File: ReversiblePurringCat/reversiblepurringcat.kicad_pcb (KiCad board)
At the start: 2 copper layers, 116 x 90.9 mm, 34 parts, among them J0 nice!view, U0 ProMicro-kbd

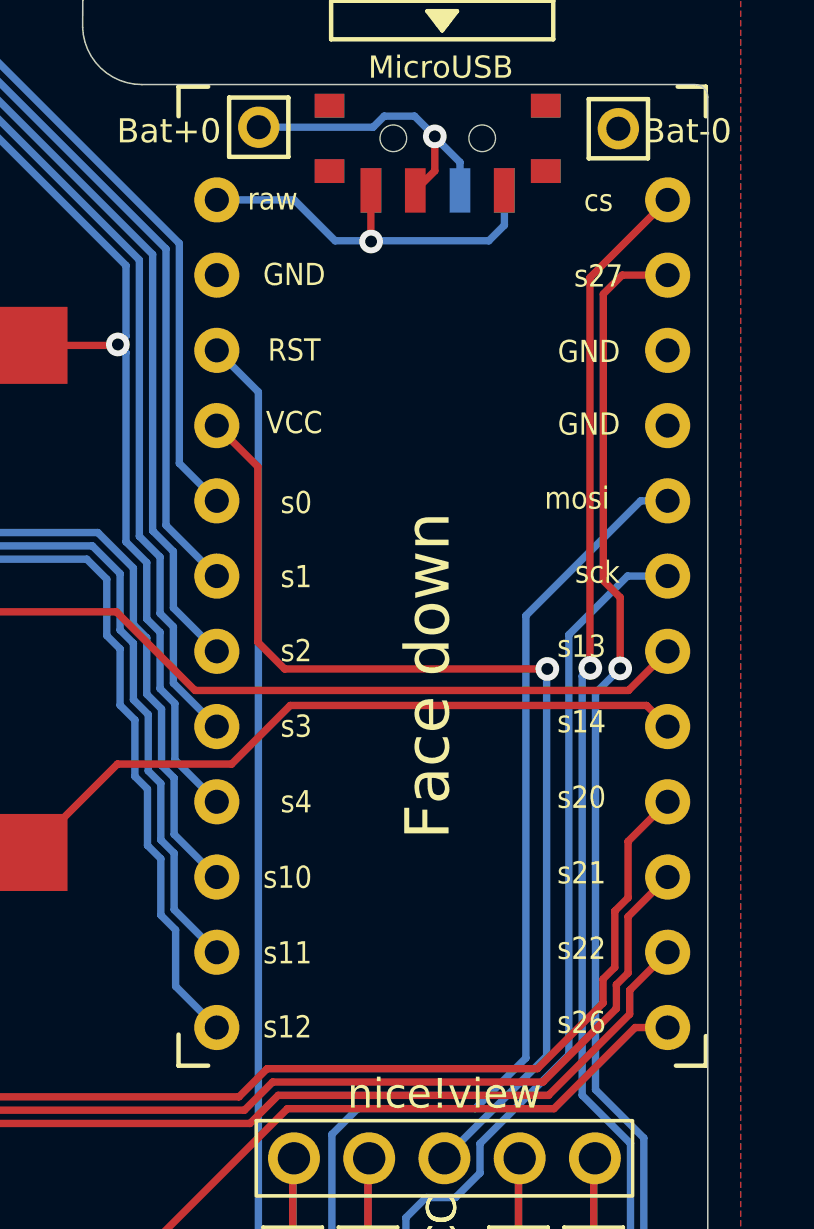
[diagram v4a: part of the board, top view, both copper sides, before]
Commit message: updated labels
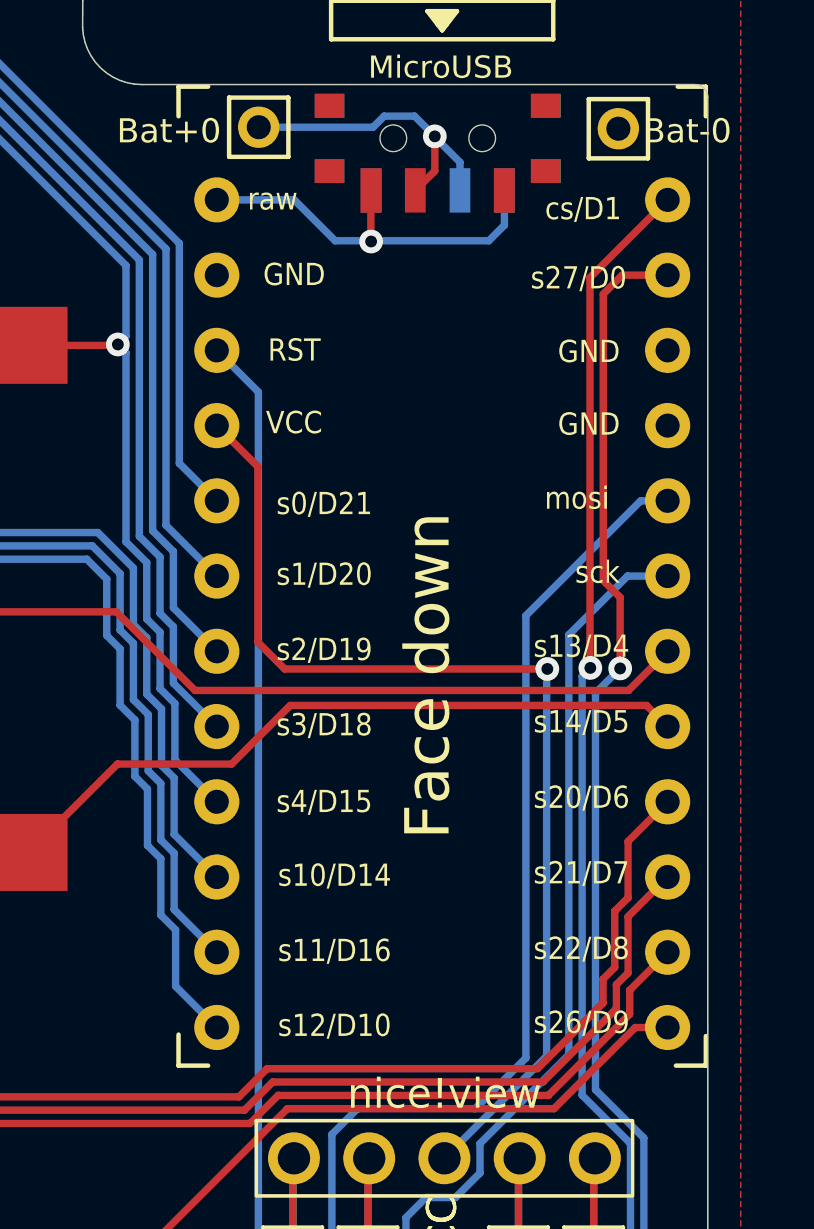
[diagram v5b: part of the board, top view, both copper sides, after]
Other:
- board text added: "s14/D5"
- board text removed: "s14"
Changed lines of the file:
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@@
 			)
 		)
-		(fp_text user "s22"
+		(fp_text user "s22/D8"
 			(at 4.705 10.8 0)
 			(unlocked yes)
@@
 			)
 		)
-		(fp_text user "s2"
-			(at -4.395 0.75 0)
+		(fp_text user "s2/D19"
+			(at -2.35184 0.710728 0)
 			(unlocked yes)
 			(layer "F.SilkS")
@@
 			)
 		)
-		(fp_text user "cs"
-			(at 5.27576 -14.45 0)
+		(fp_text user "cs/D1"
+			(at 4.76016 -14.173672 0)
 			(unlocked yes)
 			(layer "F.SilkS")
@@
 			)
 		)
-		(fp_text user "s3"
-			(at -4.395 3.3 0)
+		(fp_text user "s3/D18"
+			(at -2.35184 3.250728 0)
 			(unlocked yes)
 			(layer "F.SilkS")
@@
 			)
 		)
-		(fp_text user "s27"
-			(at 5.27576 -11.9 0)
+		(fp_text user "s27/D0"
+			(at 4.60776 -11.836872 0)
 			(unlocked yes)
 			(layer "F.SilkS")
@@
 			)
 		)
-		(fp_text user "s10"
-			(at -4.395 8.4 0)
+		(fp_text user "s10/D14"
+			(at -1.713745 8.330728 0)
 			(unlocked yes)
 			(layer "F.SilkS")
@@
 			)
 		)
-		(fp_text user "s11"
-			(at -4.395 10.95 0)
+		(fp_text user "s11/D16"
+			(at -1.713745 10.870728 0)
 			(unlocked yes)
 			(layer "F.SilkS")
@@
 			)
 		)
-		(fp_text user "s12"
-			(at -4.395 13.45 0)
+		(fp_text user "s12/D10"
+			(at -1.713745 13.3992 0)
 			(unlocked yes)
 			(layer "F.SilkS")
@@
 			)
 		)
-		(fp_text user "s26"
+		(fp_text user "s26/D9"
 			(at 4.705 13.3 0)
 			(unlocked yes)
@@
 			)
 		)
-		(fp_text user "s4"
-			(at -4.395 5.85 0)
+		(fp_text user "s4/D15"
+			(at -2.35184 5.841528 0)
 			(unlocked yes)
 			(layer "F.SilkS")
@@
 			)
 		)
-		(fp_text user "s0"
-			(at -4.395 -4.25 0)
+		(fp_text user "s0/D21"
+			(at -2.35184 -4.216872 0)
 			(unlocked yes)
 			(layer "F.SilkS")
@@
 			)
 		)
-		(fp_text user "s21"
+		(fp_text user "s21/D7"
 			(at 4.705 8.25 0)
 			(unlocked yes)
@@
 			)
 		)
-		(fp_text user "s20"
+		(fp_text user "s20/D6"
 			(at 4.705 5.7 0)
 			(unlocked yes)
@@
 			)
 		)
-		(fp_text user "s1"
-			(at -4.395 -1.75 0)
+		(fp_text user "s1/D20"
+			(at -2.35184 -1.829272 0)
 			(unlocked yes)
 			(layer "F.SilkS")
@@
 			)
 		)
-		(fp_text user "s13"
+		(fp_text user "s13/D4"
 			(at 4.705 0.6 0)
 			(unlocked yes)
@@
 		)
 		(fp_line
-			(start -6.999999 -6)
+			(start -6.999998 -6)
 			(end -7 -7)
 			(stroke
@@
 		)
 		(fp_line
-			(start -6 6.999999)
+			(start -6 6.999998)
 			(end -7 7)
 			(stroke
@@
 		(fp_line
 			(start 1.5 3.7)
-			(end -0.999999 3.7)
+			(end -0.999998 3.7)
 			(stroke
 				(width 0.15)
@@
 		)
 		(fp_line
-			(start 6 -6.999999)
+			(start 6 -6.999998)
 			(end 7 -7)
 			(stroke
@@
 		)
 		(fp_line
-			(start 6.999999 6)
+			(start 6.999998 6)
 			(end 7 7)
 			(stroke
@@
 		)
 		(fp_arc
-			(start -0.999999 3.7)
+			(start -0.999998 3.7)
 			(mid -2.060659 3.26066)
 			(end -2.5 2.2)
@@
 		)
 		(fp_line
-			(start -6.999999 -6)
+			(start -6.999998 -6)
 			(end -7 -7)
 			(stroke
@@
 		)
 		(fp_line
-			(start -6 6.999999)
+			(start -6 6.999998)
 			(end -7 7)
 			(stroke
@@
 		)
 		(fp_line
-			(start 6 -6.999999)
+			(start 6 -6.999998)
 			(end 7 -7)
 			(stroke
@@
 		)
 		(fp_line
-			(start 6.999999 6)
+			(start 6.999998 6)
 			(end 7 7)
 			(stroke
@@
 		(fp_line
 			(start 1.5 3.7)
-			(end -0.999999 3.7)
+			(end -0.999998 3.7)
 			(stroke
 				(width 0.15)
@@
 		)
 		(fp_arc
-			(start -0.999999 3.7)
+			(start -0.999998 3.7)
 			(mid -2.060659 3.26066)
 			(end -2.5 2.2)
@@
 		)
 		(fp_line
-			(start 7 4.999999)
+			(start 7 4.999998)
 			(end 9.5 5)
 			(stroke
@@
 		)
 		(fp_line
-			(start -6.999999 -6)
+			(start -6.999998 -6)
 			(end -7 -7)
 			(stroke
@@
 		)
 		(fp_line
-			(start -6 6.999999)
+			(start -6 6.999998)
 			(end -7 7)
 			(stroke
@@
 		(fp_line
 			(start 1.5 3.7)
-			(end -0.999999 3.7)
+			(end -0.999998 3.7)
 			(stroke
 				(width 0.15)
@@
 		)
 		(fp_line
-			(start 6 -6.999999)
+			(start 6 -6.999998)
 			(end 7 -7)
 			(stroke
@@
 		)
 		(fp_line
-			(start 6.999999 6)
+			(start 6.999998 6)
 			(end 7 7)
 			(stroke
@@
 		)
 		(fp_arc
-			(start -0.999999 3.7)
+			(start -0.999998 3.7)
 			(mid -2.060659 3.26066)
 			(end -2.5 2.2)
@@
 		)
 		(fp_line
-			(start -6.999999 -6)
+			(start -6.999998 -6)
 			(end -7 -7)
 			(stroke
@@
 		)
 		(fp_line
-			(start -6 6.999999)
+			(start -6 6.999998)
 			(end -7 7)
 			(stroke
@@
 		)
 		(fp_line
-			(start 6 -6.999999)
+			(start 6 -6.999998)
 			(end 7 -7)
 			(stroke
@@
 		)
 		(fp_line
-			(start 6.999999 6)
+			(start 6.999998 6)
 			(end 7 7)
 			(stroke
@@
 		(fp_line
 			(start 1.5 3.7)
-			(end -0.999999 3.7)
+			(end -0.999998 3.7)
 			(stroke
 				(width 0.15)
@@
 		)
 		(fp_arc
-			(start -0.999999 3.7)
+			(start -0.999998 3.7)
 			(mid -2.060659 3.26066)
 			(end -2.5 2.2)
@@
 		)
 		(fp_line
-			(start 2.000001 4.2)
+			(start 2.000002 4.2)
 			(end 1.5 3.7)
 			(stroke
@@
 		(fp_arc
 			(start -2.5 6.2)
-			(mid -2.146446 6.346447)
+			(mid -2.146446 6.346446)
 			(end -2 6.7)
 			(stroke
@@
 		)
 		(fp_line
-			(start 2.000001 4.2)
+			(start 2.000002 4.2)
 			(end 1.5 3.7)
 			(stroke
@@
 		(fp_arc
 			(start -2.5 6.2)
-			(mid -2.146446 6.346447)
+			(mid -2.146446 6.346446)
 			(end -2 6.7)
 			(stroke
@@
 		)
 		(pad "" np_thru_hole circle
-			(at 5.000001 3.75 5)
+			(at 5.000002 3.75 5)
 			(size 3 3)
 			(drill 3)
@@
 		)
 		(fp_line
-			(start 2.000001 4.2)
+			(start 2.000002 4.2)
 			(end 1.5 3.7)
 			(stroke
@@
 		(fp_arc
 			(start -2.5 6.2)
-			(mid -2.146446 6.346447)
+			(mid -2.146446 6.346446)
 			(end -2 6.7)
 			(stroke
@@
 		)
 		(fp_line
-			(start 2.000001 4.2)
+			(start 2.000002 4.2)
 			(end 1.5 3.7)
 			(stroke
@@
 		(fp_arc
 			(start -2.5 6.2)
-			(mid -2.146446 6.346447)
+			(mid -2.146446 6.346446)
 			(end -2 6.7)
 			(stroke
@@
 		)
 		(pad "" np_thru_hole circle
-			(at 5.000001 3.75 5)
+			(at 5.000002 3.75 5)
 			(size 3 3)
 			(drill 3)
@@
 		)
 		(fp_line
-			(start -6.999999 -6)
+			(start -6.999998 -6)
 			(end -7 -7)
 			(stroke
@@
 		)
 		(fp_line
-			(start -6 6.999999)
+			(start -6 6.999998)
 			(end -7 7)
 			(stroke
@@
 		(fp_line
 			(start 1.5 3.7)
-			(end -0.999999 3.7)
+			(end -0.999998 3.7)
 			(stroke
 				(width 0.15)
@@
 		)
 		(fp_line
-			(start 6 -6.999999)
+			(start 6 -6.999998)
 			(end 7 -7)
 			(stroke
@@
 		)
 		(fp_line
-			(start 6.999999 6)
+			(start 6.999998 6)
 			(end 7 7)
 			(stroke
@@
 		)
 		(fp_arc
-			(start -0.999999 3.7)
+			(start -0.999998 3.7)
 			(mid -2.060659 3.26066)
 			(end -2.5 2.2)
@@
 		)
 		(fp_line
-			(start -6.999999 -6)
+			(start -6.999998 -6)
 			(end -7 -7)
 			(stroke
@@
 		)
 		(fp_line
-			(start -6 6.999999)
+			(start -6 6.999998)
 			(end -7 7)
 			(stroke
@@
 		)
 		(fp_line
-			(start 6 -6.999999)
+			(start 6 -6.999998)
 			(end 7 -7)
 			(stroke
@@
 		)
 		(fp_line
-			(start 6.999999 6)
+			(start 6.999998 6)
 			(end 7 7)
 			(stroke
@@
 		(fp_line
 			(start 1.5 3.7)
-			(end -0.999999 3.7)
+			(end -0.999998 3.7)
 			(stroke
 				(width 0.15)
@@
 		)
 		(fp_arc
-			(start -0.999999 3.7)
+			(start -0.999998 3.7)
 			(mid -2.060659 3.26066)
 			(end -2.5 2.2)
@@
 		)
 	)
-	(gr_text "s14"
+	(gr_text "s14/D5"
 		(at 243.42924 56.947672 0)
 		(layer "F.SilkS")

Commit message: final before pcb order
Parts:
- moved RSW0 49.9 mm to (196.0, 93.0), turned to -12 degrees
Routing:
- net reset: track 52.6 -> 77.6 mm
- net MOSI: track 51.1 -> 55.3 mm
- net s27: track 85.4 -> 82.5 mm
- net s26: track 61.8 -> 63.4 mm
- net vcc: track 36.0 -> 35.2 mm
- net SCK: track 38.0 -> 38.7 mm
- net s1: track 112.1 -> 111.6 mm
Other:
- board text added: "say gay"
